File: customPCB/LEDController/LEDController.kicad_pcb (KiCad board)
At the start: 2 copper layers, 66 x 38 mm, 34 parts, among them J1 USB_B_Micro, J2 Barrel_Jack_MountingPin, J3 Conn_01x03, J4 Conn_01x03, J5 Conn_01x02, J6 Conn_01x02, Q1 DMG2301L, Q2 TRANS_NPN-MMBT2222AL, Q3 TRANS_NPN-MMBT2222AL, SW1 KMR2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

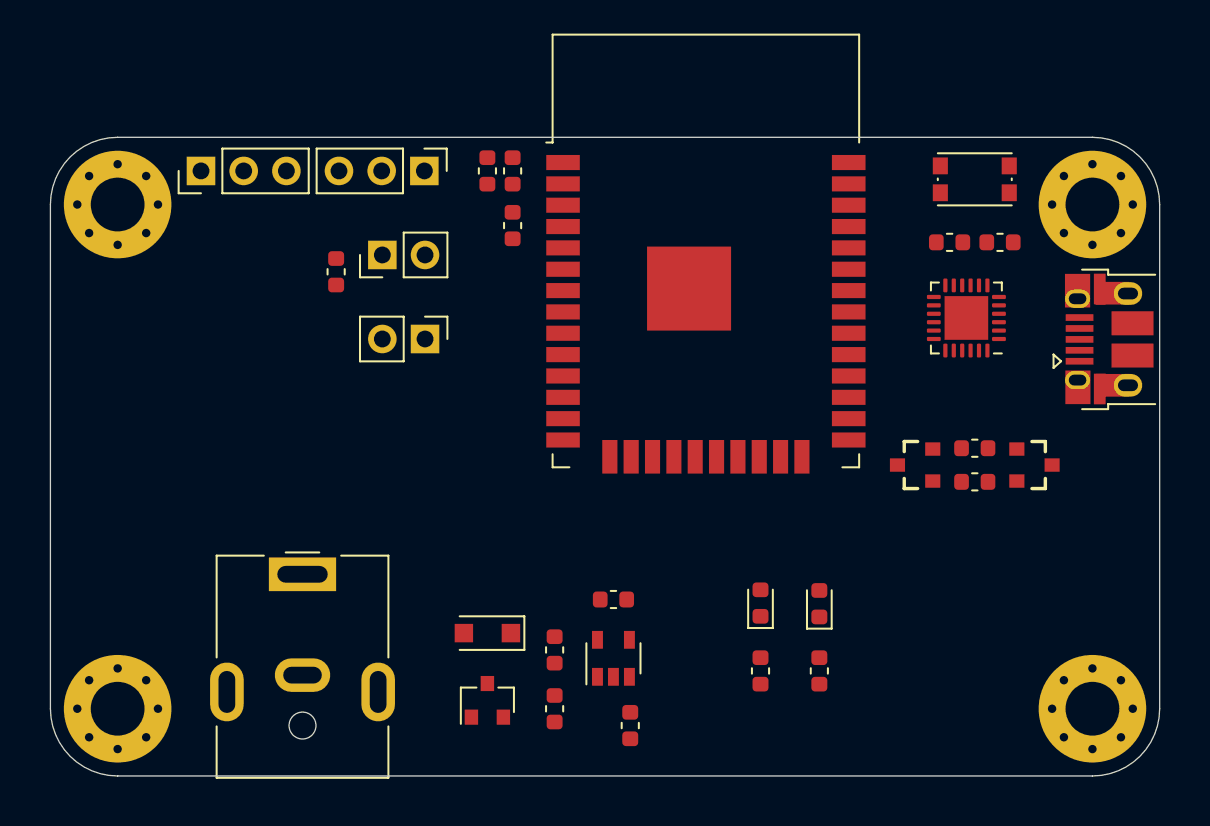
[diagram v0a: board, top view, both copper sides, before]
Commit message: added off button
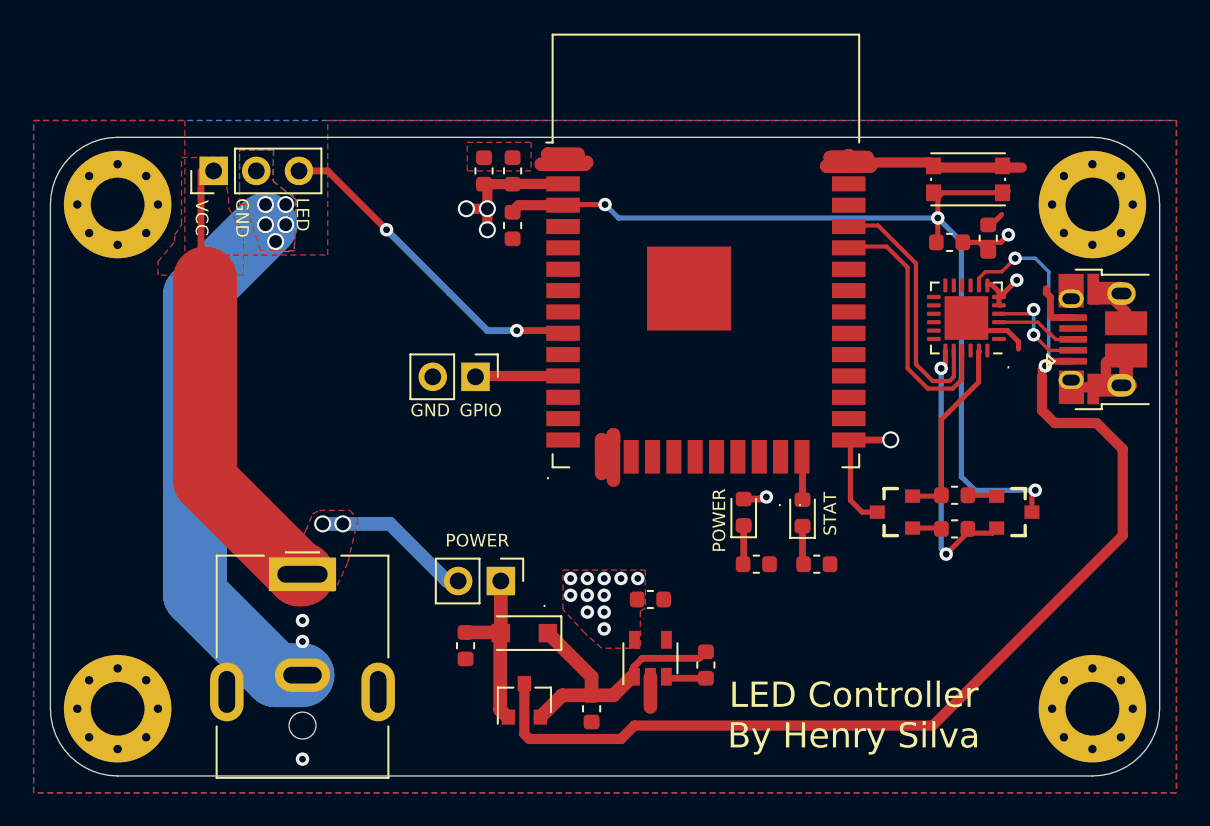
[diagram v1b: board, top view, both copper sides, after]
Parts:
- removed J4: Conn_01x03, Connector_PinHeader_2.54mm:PinHeader_1x03_P2.54mm_Vertical
- removed J5: Conn_01x02, Connector_PinHeader_2.54mm:PinHeader_1x02_P2.54mm_Vertical
- removed R5: 10K, Resistor_SMD:R_0603_1608Metric
- added G***: LOGO, logos:groyper, B.Cu at (112.2, 51.8)
- added J7: Conn_01x02, Connector_PinHeader_2.54mm:PinHeader_1x02_P2.54mm_Vertical, F.Cu at (100.8, 68.4)
- moved R3 6.35 mm to (116.0, 67.4), turned to 0 degrees
- moved R4 6.35 mm to (119.6, 67.4), turned to 0 degrees
- moved R2 5.76 mm to (113.0, 73.4), turned to 270 degrees
- moved D2 5.49 mm to (115.2, 64.3)
- moved D3 5.49 mm to (118.8, 64.3)
- moved R1 5.31 mm to (98.7, 72.2), turned to 270 degrees
- moved J6 3.75 mm to (99.3, 56.2)
- moved Q2 3.05 mm to (124.3, 64.3)
- moved R7 3.05 mm to (127.8, 65.3)
- moved R8 3.05 mm to (127.8, 63.3)
- moved Q3 3.05 mm to (131.3, 64.3)
- moved C1 2.20 mm to (106.2, 76.0)
- moved C2 2.20 mm to (109.7, 69.5)
- moved D1 2.20 mm to (102.2, 71.5)
- moved Q1 2.20 mm to (102.2, 75.5)
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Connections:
- D1 pad 2: VCC -> Net-(D1-Pad2)
- J3 pad 1: +5V -> VCC
- J3 pad 2: LED_PIN -> GND
- J3 pad 3: GND -> LED_PIN
- Q1 pad 1: VCC -> Net-(D1-Pad2)
- R1 pad 1: +5V -> Net-(D1-Pad2)
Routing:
- net GND: track 0.00 -> 81.6 mm, vias 0 -> 8
- net VBUS: track 0.00 -> 70.5 mm, vias 0 -> 2
- net RESET: track 0.00 -> 54.7 mm, vias 0 -> 3
- net VCC: track 0.00 -> 36.0 mm, vias 0 -> 2
- net LED_PIN: track 0.00 -> 19.8 mm, vias 0 -> 2
- net +3V3: track 0.00 -> 16.7 mm, vias 0 -> 17
- net +5V: track 0.00 -> 16.2 mm
- net RTS: track 0.00 -> 16.0 mm, vias 0 -> 2
- net RXD0: track 0.00 -> 15.7 mm
- net TXD0: track 0.00 -> 15.3 mm
- net DTR: track 0.00 -> 11.4 mm
- net Net-(D1-Pad2): track 0.00 -> 9.68 mm
- net BOOT: track 0.00 -> 7.99 mm, vias 0 -> 1
- net D-: track 0.00 -> 6.34 mm, vias 0 -> 2
- net GPIO: track 0.00 -> 5.27 mm
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- added copper zone on B.Cu, net +3V3
- added copper zone on F.Cu, net +3V3
- added copper zone on B.Cu, net GND
- added copper zone on F.Cu, net GND
- added copper zone on F.Cu, net VCC
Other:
- board text added: "."
- board text added: "GND"
- board text added: "GPIO"
- board text added: "LED"
- board text added: "LED Controller By Henry Silva"
- board text added: "POWER"
- board text added: "STAT"
- board text added: "VCC"
